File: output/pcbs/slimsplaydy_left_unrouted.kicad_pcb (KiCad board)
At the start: 2 copper layers, 122.3 x 94.4 mm, 44 parts

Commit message: Finish layout, schematic, routing.
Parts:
- removed MH16, MH17, MH18, MH19, MH20: , ceoloide:mounting_hole_npth
- removed PAD1, PAD2: , SMDPad
- removed XX1: , Battery_301230
- added MAG1: , magsafe, B.Cu at (45.0, -32.5)
- CONN1: footprint ceoloide:battery_connector_molex_pico_ezmate_1x02 -> Molex_Pico_EZMate_Plus_1x02
- moved MH3 251.8 mm to (35.0, -64.8)
- moved MH2 244.3 mm to (-13.0, -15.3), turned to 8 degrees
- moved MH5 228.5 mm to (101.5, -55.5)
- moved MH13 227.9 mm to (-15.9, -42.7), turned to 8 degrees
- moved MH4 225.5 mm to (77.0, -57.8)
- moved MH6 218.0 mm to (90.0, -21.5), turned to 0 degrees
- moved MH14 201.5 mm to (2.96, -51.8), turned to 3 degrees
- moved MH12 194.3 mm to (-7.92, 11.9), turned to 8 degrees
- moved MH7 187.6 mm to (82.5, 0.55), turned to 0 degrees
- moved S4 180.6 mm to (17.0, -13.5), turned to 3 degrees
- moved S5 180.1 mm to (16.1, -30.5), turned to 3 degrees
- moved MH10 179.8 mm to (29.0, -8.95), turned to 0 degrees
- moved S6 179.6 mm to (15.2, -47.4), turned to 3 degrees
- moved CONN1 179.5 mm to (40.0, -8.45), turned to 0 degrees
- moved S1 178.9 mm to (0.00, 0.00), turned to 8 degrees
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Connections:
- net hand_index_top renamed finger_index_top
- net hand_inner_top renamed finger_inner_top
- net hand_middle_top renamed finger_middle_top
- MCU1 pad 1: D1 -> finger_inner_home
- MCU1 pad 10: hand_pinky_home -> finger_pinky_top
- MCU1 pad 11: hand_middle_bottom -> thumb_tucky_fan
- MCU1 pad 12: hand_pinky_top -> thumb_reachy_fan
- MCU1 pad 13: hand_ring_home -> finger_index_home
- MCU1 pad 14: hand_ring_top -> finger_middle_home
- MCU1 pad 15: hand_inner_home -> finger_ring_home
- MCU1 pad 16: hand_index_home -> finger_pinky_home
- MCU1 pad 17: hand_middle_home -> finger_ring_top
- MCU1 pad 2: thumb_far_fan -> D0
- MCU1 pad 5: thumb_near_fan -> finger_pinky_bottom
- MCU1 pad 6: hand_pinky_bottom -> finger_ring_bottom
- MCU1 pad 7: hand_ring_bottom -> finger_middle_bottom
- MCU1 pad 8: hand_inner_bottom -> finger_index_bottom
- MCU1 pad 9: hand_index_bottom -> finger_inner_bottom
- S1 pad : GND -> (no net)
- S1 pad 1: hand_pinky_bottom -> finger_pinky_bottom
- S10 pad : GND -> (no net)
- S10 pad 1: hand_index_bottom -> finger_index_bottom
- S11 pad : GND -> (no net)
- S11 pad 1: hand_index_home -> finger_index_home
- S12 pad : GND -> (no net)
- S13 pad : GND -> (no net)
- S13 pad 1: hand_inner_bottom -> finger_inner_bottom
- S14 pad : GND -> (no net)
- S14 pad 1: hand_inner_home -> finger_inner_home
- S15 pad : GND -> (no net)
- S16 pad : GND -> (no net)
- S16 pad 1: thumb_near_fan -> thumb_tucky_fan
- S17 pad : GND -> (no net)
- S17 pad 1: thumb_far_fan -> thumb_reachy_fan
- S2 pad : GND -> (no net)
- S2 pad 1: hand_pinky_home -> finger_pinky_home
- S3 pad : GND -> (no net)
- S3 pad 1: hand_pinky_top -> finger_pinky_top
- S4 pad : GND -> (no net)
- S4 pad 1: hand_ring_bottom -> finger_ring_bottom
- S5 pad : GND -> (no net)
- S5 pad 1: hand_ring_home -> finger_ring_home
- S6 pad : GND -> (no net)
- S6 pad 1: hand_ring_top -> finger_ring_top
- S7 pad : GND -> (no net)
- S7 pad 1: hand_middle_bottom -> finger_middle_bottom
- S8 pad : GND -> (no net)
- S8 pad 1: hand_middle_home -> finger_middle_home
- S9 pad : GND -> (no net)
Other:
- board size 122.3 x 94.4 mm -> 122.6 x 97.5 mm

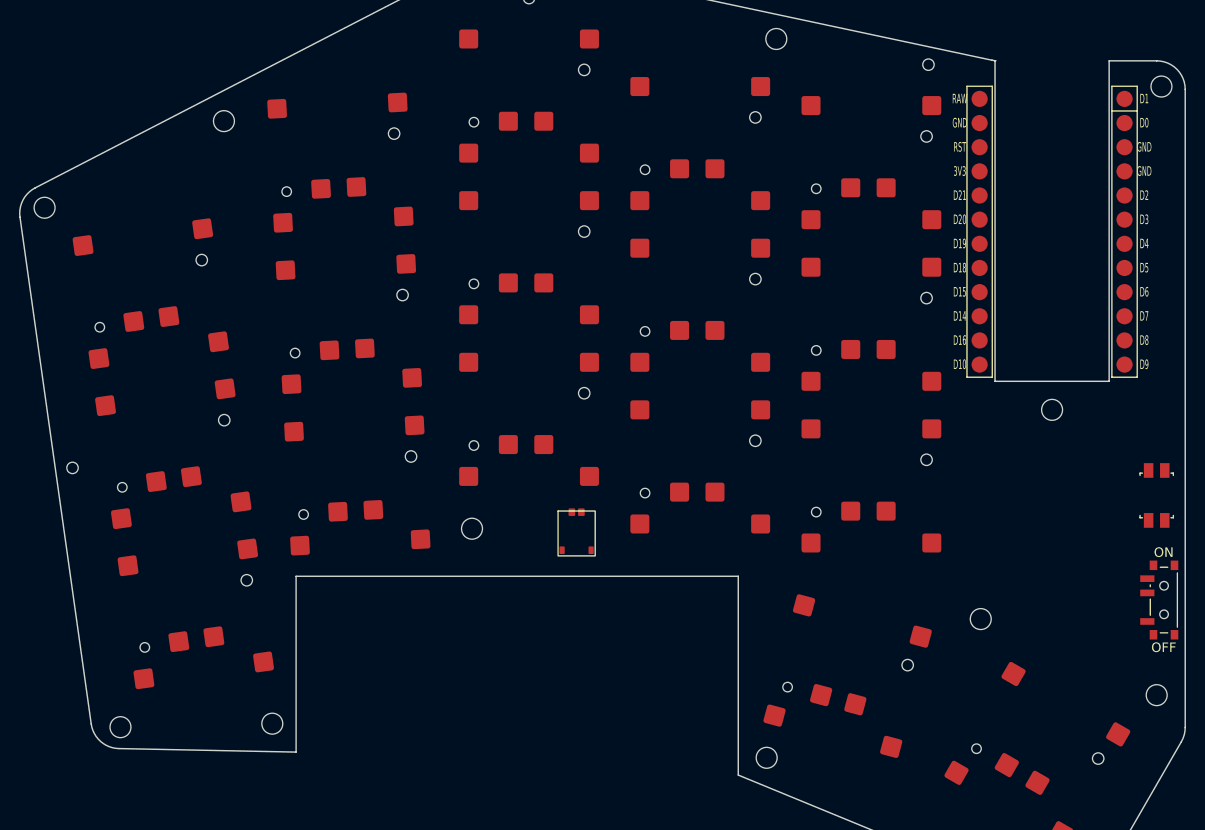
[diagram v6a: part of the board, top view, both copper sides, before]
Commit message: Fix MCU slots. Fillet outline. Reroute both sides. Re-re-reroute both sides.
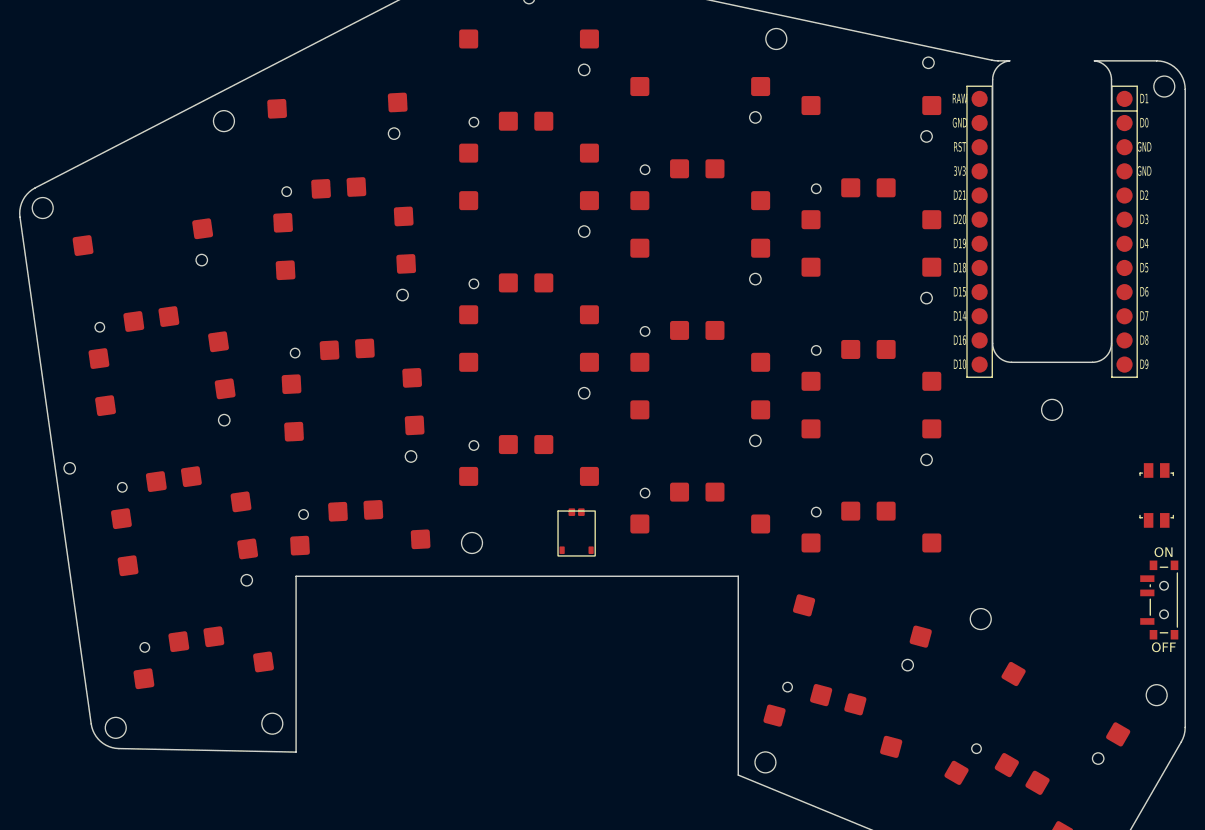
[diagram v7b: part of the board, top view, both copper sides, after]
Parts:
- moved MH10 1.50 mm to (29.0, -7.45)
- moved MH9 0.50 mm to (59.9, 15.6)
- moved MH12 0.50 mm to (-8.41, 12.0)
- moved MH2 0.30 mm to (-13.3, -15.3)
- moved MH5 0.30 mm to (101.8, -55.5)
- moved MH4 0.20 mm to (77.0, -58.0)
- moved MH13 0.20 mm to (-16.1, -42.7)
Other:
- outline, holes or cut-outs redrawn
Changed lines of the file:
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@@
   (title_block
     (title "slimsplaydy_left_unrouted")
-    (date "2025-06-13")
+    (date "2025-06-14")
     (rev "0.1")
     (company "huntercook")
@@
   (footprint "ceoloide:mounting_hole_npth"
     (layer "F.Cu")
-    (at -12.961810999999999 -15.345405 8)
+    (at -13.258891499999999 -15.303653099999998 8)
     (property "Reference" "MH2"
       (at 0 2.55 8)
@@
   (footprint "ceoloide:mounting_hole_npth"
     (layer "F.Cu")
-    (at 77.0478765 -57.7502446 0)
+    (at 77.0478765 -57.950244600000005 0)
     (property "Reference" "MH4"
       (at 0 2.55 0)
@@
   (footprint "ceoloide:mounting_hole_npth"
     (layer "F.Cu")
-    (at 101.5478765 -55.450244600000005 0)
+    (at 101.8478765 -55.450244600000005 0)
     (property "Reference" "MH5"
       (at 0 2.55 0)
@@
   (footprint "ceoloide:mounting_hole_npth"
     (layer "F.Cu")
-    (at 60.0347216 15.139062299999999 -15)
+    (at 59.905312 15.6220252 -15)
     (property "Reference" "MH9"
       (at 0 2.55 -15)
@@
   (footprint "ceoloide:mounting_hole_npth"
     (layer "F.Cu")
-    (at 29.0478764 -8.9502445 0)
+    (at 29.0478764 -7.4502445 0)
     (property "Reference" "MH10"
       (at 0 2.55 0)
@@
   (footprint "ceoloide:mounting_hole_npth"
     (layer "F.Cu")
-    (at -7.9183945 11.9180128 8)
+    (at -8.4135285 11.9875993 8)
     (property "Reference" "MH12"
       (at 0 2.55 8)
@@
   (footprint "ceoloide:mounting_hole_npth"
     (layer "F.Cu")
-    (at -15.897829999999999 -42.703032699999994 8)
+    (at -16.0958836 -42.675198099999996 8)
     (property "Reference" "MH13"
       (at 0 2.55 8)
@@
 (gr_line (start 25.7768870313585 -66.4502445) (end 44.732180690054186 -66.4502445) (layer Edge.Cuts) (stroke (width 0.15) (type default)))
 (gr_line (start 45.35665676969428 -66.38452970433299) (end 83.73909613030581 -58.21595939566699) (layer Edge.Cuts) (stroke (width 0.15) (type default)))
-(gr_line (start 96.0478765 -58.15024460000001) (end 101.0478765 -58.15024460000001) (layer Edge.Cuts) (stroke (width 0.15) (type default)))
+(gr_line (start 84.3635722099459 -58.15024460000001) (end 85.5981267 -58.15024460000001) (layer Edge.Cuts) (stroke (width 0.15) (type default)))
+(gr_line (start 94.49762630000001 -58.15024460000001) (end 101.0478765 -58.15024460000001) (layer Edge.Cuts) (stroke (width 0.15) (type default)))
 (gr_line (start 104.0478765 -55.15024460000001) (end 104.0478765 11.946543806493537) (layer Edge.Cuts) (stroke (width 0.15) (type default)))
 (gr_arc (start 90.6457768654196 30.77590257780282) (mid 92.7553924654196 30.84087507780282) (end 94.38570266541961 29.50043177780282) (layer Edge.Cuts) (stroke (width 0.15) (type default)))
@@
 (gr_arc (start 25.7768870313585 -66.4502445) (mid 25.068492131358497 -66.36540769999999) (end 24.4001624313585 -66.1156956) (layer Edge.Cuts) (stroke (width 0.15) (type default)))
 (gr_arc (start 45.35665679005419 -66.3845297) (mid 45.04614279005418 -66.4337706) (end 44.732180690054186 -66.4502445) (layer Edge.Cuts) (stroke (width 0.15) (type default)))
-(gr_arc (start 83.7390961099459 -58.21595940000001) (mid 83.9280699099459 -58.182023300000004) (end 84.1188274099459 -58.160244600000006) (layer Edge.Cuts) (stroke (width 0.15) (type default)))
+(gr_arc (start 83.7390961099459 -58.21595940000001) (mid 84.0496101099459 -58.16671850000001) (end 84.3635722099459 -58.15024460000001) (layer Edge.Cuts) (stroke (width 0.15) (type default)))
 (gr_arc (start 104.0478765 -55.15024460000001) (mid 103.1691968 -57.27156490000001) (end 101.0478765 -58.15024460000001) (layer Edge.Cuts) (stroke (width 0.15) (type default)))
 (gr_arc (start 103.6465458 13.445516006493538) (mid 103.9458075 12.722427806493537) (end 104.0478765 11.946543806493537) (layer Edge.Cuts) (stroke (width 0.15) (type default)))
-(gr_line (start 84.1188274099459 -58.160244600000006) (end 84.0478765 -58.160244600000006) (layer Edge.Cuts) (stroke (width 0.15) (type default)))
-(gr_line (start 84.0478765 -58.160244600000006) (end 84.0478765 -24.450244600000005) (layer Edge.Cuts) (stroke (width 0.15) (type default)))
-(gr_line (start 84.0478765 -24.450244600000005) (end 96.0478765 -24.450244600000005) (layer Edge.Cuts) (stroke (width 0.15) (type default)))
-(gr_line (start 96.0478765 -24.450244600000005) (end 96.0478765 -58.15024460000001) (layer Edge.Cuts) (stroke (width 0.15) (type default)))
+(gr_line (start 83.7978765 -56.160244600000006) (end 83.7978765 -28.450244600000005) (layer Edge.Cuts) (stroke (width 0.15) (type default)))
+(gr_line (start 85.7978765 -26.450244600000005) (end 94.2978765 -26.450244600000005) (layer Edge.Cuts) (stroke (width 0.15) (type default)))
+(gr_line (start 96.2978765 -28.450244600000005) (end 96.2978765 -56.160244600000006) (layer Edge.Cuts) (stroke (width 0.15) (type default)))
+(gr_arc (start 85.5981267 -58.15024460000001) (mid 84.31472120000001 -57.50197860000001) (end 83.7978765 -56.160244600000006) (layer Edge.Cuts) (stroke (width 0.15) (type default)))
+(gr_arc (start 83.7978765 -28.450244600000005) (mid 84.3836629 -27.036031000000005) (end 85.7978765 -26.450244600000005) (layer Edge.Cuts) (stroke (width 0.15) (type default)))
+(gr_arc (start 94.2978765 -26.450244600000005) (mid 95.7120901 -27.036031000000005) (end 96.2978765 -28.450244600000005) (layer Edge.Cuts) (stroke (width 0.15) (type default)))
+(gr_arc (start 96.2978765 -56.160244600000006) (mid 95.7810319 -57.50197860000001) (end 94.49762630000001 -58.15024460000001) (layer Edge.Cuts) (stroke (width 0.15) (type default)))
 (gr_line (start 10.5478764 14.539434268083982) (end 10.5478764 -3.9502445) (layer Edge.Cuts) (stroke (width 0.15) (type default)))
 (gr_line (start 10.5478764 -3.9502445) (end 57.0478764 -3.9502445) (layer Edge.Cuts) (stroke (width 0.15) (type default)))

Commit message: Add production files.
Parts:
- moved MCU1 0.20 mm to (90.0, -41.7)
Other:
- outline, holes or cut-outs redrawn
